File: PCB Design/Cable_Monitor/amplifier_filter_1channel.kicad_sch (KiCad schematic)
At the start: 6 parts, among them U7 MCP6002-xSN

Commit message: PCB Layout Update
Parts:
- renumbered C10 to C16, R18 to R15, R19 to R16, R20 to R17, R21 to R18, U7 to U5
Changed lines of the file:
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@@
   (symbol (lib_id "Amplifier_Operational:MCP6002-xSN") (at 93.98 50.8 0) (unit 1)
     (in_bom yes) (on_board yes) (dnp no) (fields_autoplaced)
-    (property "Reference" "U7" (at 93.98 40.64 0)
+    (property "Reference" "U5" (at 93.98 40.64 0)
       (effects (font (size 1.27 1.27)))
     )
@@
       (project "Cable_Monitor"
         (path "/1f276d59-ad9b-4e70-a842-f3b7e562eb9b/de01ffac-1f9d-4a03-9ae5-48822ed64956"
-          (reference "U7") (unit 1)
-        )
-        (path "/1f276d59-ad9b-4e70-a842-f3b7e562eb9b/dcec0d15-a185-46c1-b70e-bab38dd94215"
-          (reference "U1") (unit 1)
+          (reference "U5") (unit 1)
+        )
+        (path "/1f276d59-ad9b-4e70-a842-f3b7e562eb9b/dcec0d15-a185-46c1-b70e-bab38dd94215"
+          (reference "U6") (unit 1)
         )
       )
@@
   (symbol (lib_id "Device:R") (at 104.14 66.04 0) (unit 1)
     (in_bom yes) (on_board yes) (dnp no) (fields_autoplaced)
-    (property "Reference" "R19" (at 106.68 64.7699 0)
+    (property "Reference" "R16" (at 106.68 64.7699 0)
       (effects (font (size 1.27 1.27)) (justify left))
     )
@@
       (project "Cable_Monitor"
         (path "/1f276d59-ad9b-4e70-a842-f3b7e562eb9b/de01ffac-1f9d-4a03-9ae5-48822ed64956"
-          (reference "R19") (unit 1)
-        )
-        (path "/1f276d59-ad9b-4e70-a842-f3b7e562eb9b/dcec0d15-a185-46c1-b70e-bab38dd94215"
-          (reference "R2") (unit 1)
+          (reference "R16") (unit 1)
+        )
+        (path "/1f276d59-ad9b-4e70-a842-f3b7e562eb9b/dcec0d15-a185-46c1-b70e-bab38dd94215"
+          (reference "R20") (unit 1)
         )
       )
@@
   (symbol (lib_id "Device:R") (at 154.94 66.04 0) (unit 1)
     (in_bom yes) (on_board yes) (dnp no) (fields_autoplaced)
-    (property "Reference" "R21" (at 157.48 64.7699 0)
+    (property "Reference" "R18" (at 157.48 64.7699 0)
       (effects (font (size 1.27 1.27)) (justify left))
     )
@@
       (project "Cable_Monitor"
         (path "/1f276d59-ad9b-4e70-a842-f3b7e562eb9b/de01ffac-1f9d-4a03-9ae5-48822ed64956"
-          (reference "R21") (unit 1)
-        )
-        (path "/1f276d59-ad9b-4e70-a842-f3b7e562eb9b/dcec0d15-a185-46c1-b70e-bab38dd94215"
-          (reference "R4") (unit 1)
+          (reference "R18") (unit 1)
+        )
+        (path "/1f276d59-ad9b-4e70-a842-f3b7e562eb9b/dcec0d15-a185-46c1-b70e-bab38dd94215"
+          (reference "R22") (unit 1)
         )
       )
@@
   (symbol (lib_id "Amplifier_Operational:MCP6002-xSN") (at 144.78 50.8 0) (unit 2)
     (in_bom yes) (on_board yes) (dnp no) (fields_autoplaced)
-    (property "Reference" "U7" (at 144.78 40.64 0)
+    (property "Reference" "U5" (at 144.78 40.64 0)
       (effects (font (size 1.27 1.27)))
     )
@@
       (project "Cable_Monitor"
         (path "/1f276d59-ad9b-4e70-a842-f3b7e562eb9b/de01ffac-1f9d-4a03-9ae5-48822ed64956"
-          (reference "U7") (unit 2)
-        )
-        (path "/1f276d59-ad9b-4e70-a842-f3b7e562eb9b/dcec0d15-a185-46c1-b70e-bab38dd94215"
-          (reference "U1") (unit 2)
+          (reference "U5") (unit 2)
+        )
+        (path "/1f276d59-ad9b-4e70-a842-f3b7e562eb9b/dcec0d15-a185-46c1-b70e-bab38dd94215"
+          (reference "U6") (unit 2)
         )
       )
@@
   (symbol (lib_id "Device:C") (at 88.9 132.08 0) (unit 1)
     (in_bom yes) (on_board yes) (dnp no) (fields_autoplaced)
-    (property "Reference" "C10" (at 92.71 130.8099 0)
+    (property "Reference" "C16" (at 92.71 130.8099 0)
       (effects (font (size 1.27 1.27)) (justify left))
     )
@@
       (project "Cable_Monitor"
         (path "/1f276d59-ad9b-4e70-a842-f3b7e562eb9b/de01ffac-1f9d-4a03-9ae5-48822ed64956"
-          (reference "C10") (unit 1)
-        )
-        (path "/1f276d59-ad9b-4e70-a842-f3b7e562eb9b/dcec0d15-a185-46c1-b70e-bab38dd94215"
-          (reference "C2") (unit 1)
+          (reference "C16") (unit 1)
+        )
+        (path "/1f276d59-ad9b-4e70-a842-f3b7e562eb9b/dcec0d15-a185-46c1-b70e-bab38dd94215"
+          (reference "C17") (unit 1)
         )
       )
@@
   (symbol (lib_id "power:GND") (at 101.6 139.7 0) (unit 1)
     (in_bom yes) (on_board yes) (dnp no) (fields_autoplaced)
-    (property "Reference" "#PWR049" (at 101.6 146.05 0)
+    (property "Reference" "#PWR031" (at 101.6 146.05 0)
       (effects (font (size 1.27 1.27)) hide)
     )
@@
       (project "Cable_Monitor"
         (path "/1f276d59-ad9b-4e70-a842-f3b7e562eb9b/de01ffac-1f9d-4a03-9ae5-48822ed64956"
-          (reference "#PWR049") (unit 1)
-        )
-        (path "/1f276d59-ad9b-4e70-a842-f3b7e562eb9b/dcec0d15-a185-46c1-b70e-bab38dd94215"
-          (reference "#PWR013") (unit 1)
+          (reference "#PWR031") (unit 1)
+        )
+        (path "/1f276d59-ad9b-4e70-a842-f3b7e562eb9b/dcec0d15-a185-46c1-b70e-bab38dd94215"
+          (reference "#PWR035") (unit 1)
         )
       )
@@
   (symbol (lib_id "Device:R") (at 154.94 55.88 0) (unit 1)
     (in_bom yes) (on_board yes) (dnp no) (fields_autoplaced)
-    (property "Reference" "R20" (at 157.48 54.6099 0)
+    (property "Reference" "R17" (at 157.48 54.6099 0)
       (effects (font (size 1.27 1.27)) (justify left))
     )
@@
       (project "Cable_Monitor"
         (path "/1f276d59-ad9b-4e70-a842-f3b7e562eb9b/de01ffac-1f9d-4a03-9ae5-48822ed64956"
-          (reference "R20") (unit 1)
-        )
-        (path "/1f276d59-ad9b-4e70-a842-f3b7e562eb9b/dcec0d15-a185-46c1-b70e-bab38dd94215"
-          (reference "R3") (unit 1)
+          (reference "R17") (unit 1)
+        )
+        (path "/1f276d59-ad9b-4e70-a842-f3b7e562eb9b/dcec0d15-a185-46c1-b70e-bab38dd94215"
+          (reference "R21") (unit 1)
         )
       )
@@
   (symbol (lib_id "Device:R") (at 104.14 55.88 0) (unit 1)
     (in_bom yes) (on_board yes) (dnp no) (fields_autoplaced)
-    (property "Reference" "R18" (at 106.68 54.6099 0)
+    (property "Reference" "R15" (at 106.68 54.6099 0)
       (effects (font (size 1.27 1.27)) (justify left))
     )
@@
       (project "Cable_Monitor"
         (path "/1f276d59-ad9b-4e70-a842-f3b7e562eb9b/de01ffac-1f9d-4a03-9ae5-48822ed64956"
-          (reference "R18") (unit 1)
-        )
-        (path "/1f276d59-ad9b-4e70-a842-f3b7e562eb9b/dcec0d15-a185-46c1-b70e-bab38dd94215"
-          (reference "R1") (unit 1)
+          (reference "R15") (unit 1)
+        )
+        (path "/1f276d59-ad9b-4e70-a842-f3b7e562eb9b/dcec0d15-a185-46c1-b70e-bab38dd94215"
+          (reference "R19") (unit 1)
         )
       )
@@
   (symbol (lib_id "power:GND") (at 154.94 69.85 0) (unit 1)
     (in_bom yes) (on_board yes) (dnp no) (fields_autoplaced)
-    (property "Reference" "#PWR051" (at 154.94 76.2 0)
+    (property "Reference" "#PWR033" (at 154.94 76.2 0)
       (effects (font (size 1.27 1.27)) hide)
     )
@@
       (project "Cable_Monitor"
         (path "/1f276d59-ad9b-4e70-a842-f3b7e562eb9b/de01ffac-1f9d-4a03-9ae5-48822ed64956"
-          (reference "#PWR051") (unit 1)
-        )
-        (path "/1f276d59-ad9b-4e70-a842-f3b7e562eb9b/dcec0d15-a185-46c1-b70e-bab38dd94215"
-          (reference "#PWR015") (unit 1)
+          (reference "#PWR033") (unit 1)
+        )
+        (path "/1f276d59-ad9b-4e70-a842-f3b7e562eb9b/dcec0d15-a185-46c1-b70e-bab38dd94215"
+          (reference "#PWR037") (unit 1)
         )
       )
@@
   (symbol (lib_id "Amplifier_Operational:MCP6002-xSN") (at 104.14 132.08 0) (unit 3)
     (in_bom yes) (on_board yes) (dnp no) (fields_autoplaced)
-    (property "Reference" "U7" (at 102.87 130.8099 0)
+    (property "Reference" "U5" (at 102.87 130.8099 0)
       (effects (font (size 1.27 1.27)) (justify left))
     )
@@
       (project "Cable_Monitor"
         (path "/1f276d59-ad9b-4e70-a842-f3b7e562eb9b/de01ffac-1f9d-4a03-9ae5-48822ed64956"
-          (reference "U7") (unit 3)
-        )
-        (path "/1f276d59-ad9b-4e70-a842-f3b7e562eb9b/dcec0d15-a185-46c1-b70e-bab38dd94215"
-          (reference "U1") (unit 3)
+          (reference "U5") (unit 3)
+        )
+        (path "/1f276d59-ad9b-4e70-a842-f3b7e562eb9b/dcec0d15-a185-46c1-b70e-bab38dd94215"
+          (reference "U6") (unit 3)
         )
       )
@@
   (symbol (lib_id "power:+3V0") (at 101.6 124.46 0) (unit 1)
     (in_bom yes) (on_board yes) (dnp no)
-    (property "Reference" "#PWR048" (at 101.6 128.27 0)
+    (property "Reference" "#PWR030" (at 101.6 128.27 0)
       (effects (font (size 1.27 1.27)) hide)
     )
@@
       (project "Cable_Monitor"
         (path "/1f276d59-ad9b-4e70-a842-f3b7e562eb9b/de01ffac-1f9d-4a03-9ae5-48822ed64956"
-          (reference "#PWR048") (unit 1)
-        )
-        (path "/1f276d59-ad9b-4e70-a842-f3b7e562eb9b/dcec0d15-a185-46c1-b70e-bab38dd94215"
-          (reference "#PWR012") (unit 1)
+          (reference "#PWR030") (unit 1)
+        )
+        (path "/1f276d59-ad9b-4e70-a842-f3b7e562eb9b/dcec0d15-a185-46c1-b70e-bab38dd94215"
+          (reference "#PWR034") (unit 1)
         )
       )
@@
   (symbol (lib_id "power:GND") (at 104.14 69.85 0) (unit 1)
     (in_bom yes) (on_board yes) (dnp no) (fields_autoplaced)
-    (property "Reference" "#PWR050" (at 104.14 76.2 0)
+    (property "Reference" "#PWR032" (at 104.14 76.2 0)
       (effects (font (size 1.27 1.27)) hide)
     )
@@
       (project "Cable_Monitor"
         (path "/1f276d59-ad9b-4e70-a842-f3b7e562eb9b/de01ffac-1f9d-4a03-9ae5-48822ed64956"
-          (reference "#PWR050") (unit 1)
-        )
-        (path "/1f276d59-ad9b-4e70-a842-f3b7e562eb9b/dcec0d15-a185-46c1-b70e-bab38dd94215"
-          (reference "#PWR014") (unit 1)
-        )
-      )
+          (reference "#PWR032") (unit 1)
+        )
+        (path "/1f276d59-ad9b-4e70-a842-f3b7e562eb9b/dcec0d15-a185-46c1-b70e-bab38dd94215"
+          (reference "#PWR036") (unit 1)
+        )
+      )

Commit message: PCB Design Update
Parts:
- removed R15: 10k, Resistor_SMD:R_0805_2012Metric_Pad1.20x1.40mm_HandSolder, symbol Device:R
- removed R16: 1k, Resistor_SMD:R_0805_2012Metric_Pad1.20x1.40mm_HandSolder, symbol Device:R
- removed unit 1 of U5
- added C16, C17, C22, C23: 0.16uF, symbol Device:C
- added C18, C19, C20, C21: 10uF, symbol Device:C
- added R11, R12, R19, R20: 10k, symbol Device:R
- added R13, R14: 100k, symbol Device:R
- added R17: 1M, Resistor_SMD:R_0805_2012Metric_Pad1.20x1.40mm_HandSolder, symbol Device:R
- added R18: 1k, Resistor_SMD:R_0805_2012Metric_Pad1.20x1.40mm_HandSolder, symbol Device:R
- added unit 2 of U7
- R15: renamed from R17; value 12k -> 1M
- renumbered C16 to C15, R18 to R16, U5 to U7
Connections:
- net GND: now also C16.1, C17.1, C20.2, C21.2, C22.2, C23.2; no longer R16.2
- net at R15.2, R16.1: now also U7.2 (-); no longer U7.6 (-)
- net out: no longer names the net of R15.1
- net out: now also U7.1, R19.1; no longer U7.7
- new net: C20.1, R16.2
- new net: C19.2, R14.1, U7.5 (+)
- new net: R17.2, R18.1, U7.6 (-)
- new net: R17.1, R20.1, U7.7
- new net: C16.2, C18.1, R11.2
- new net: C17.2, C19.1, R12.2
- new net: C18.2, R13.1, U7.3 (+)
- new net: C21.1, R18.2
- new net VGND: R13.2, R14.2
- new net in_left: R11.1
- new net in_right: R12.1
- new net out_left: C22.1, R19.2
- new net out_right: C23.1, R20.2
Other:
- note added: "1.5V"
- moved on the sheet: C15, R15, R16, U7A, U7C

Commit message: Letzte Anpassungen am Schema
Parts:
- renumbered R11 to R14, R12 to R15, R13 to R16, R14 to R17, R15 to R18, R16 to R19, R17 to R20, R18 to R21, R19 to R22, R20 to R23

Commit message: Schema Updates, bald Fertig
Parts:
- added TP13: HS_left_VGND, TestPoint:TestPoint_Loop_D2.60mm_Drill1.6mm_Beaded, symbol Connector:TestPoint
- added TP13: HS_right_VGND, TestPoint:TestPoint_Loop_D2.60mm_Drill1.6mm_Beaded, symbol Connector:TestPoint
- C16, C17, C18, C19, C20, C21, C22, C23: footprint (none) -> Capacitor_SMD:C_0805_2012Metric_Pad1.18x1.45mm_HandSolder
- R14, R15, R16, R17, R22, R23: footprint (none) -> Resistor_SMD:R_0805_2012Metric_Pad1.20x1.40mm_HandSolder
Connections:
- net at C19.2, R17.1, U7.5 (+): now also TP13.1
- net at C18.2, R16.1, U7.3 (+): now also TP13.1
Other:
- moved on the sheet: R17

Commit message: Update
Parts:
- renumbered R14 to R17, R15 to R18, R16 to R19, R17 to R20, R18 to R21, R19 to R22, R20 to R23, R21 to R24, R22 to R25, R23 to R26
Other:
- note added: "Filtering and Amplification used for Hall-Sensors. The Hall-Sensors will be used to measure a magnetic Field and thus allow us to calculate a current."
- note added: "Supply Voltage for OP-Amp"
- note removed: "Some often used components are included here. Delete the components that are not used. Copy the components that are needed more than once."
- note removed: "Use this template if two opamps are used for better amplification and filtering. As dual opamps are used, one channel only can be handled by this sheet."
- company: hhrt@zhaw.ch -> ZHAW
- title: Amplifiers and Filters -> Amplifiers and Filters for Hall-Sensor

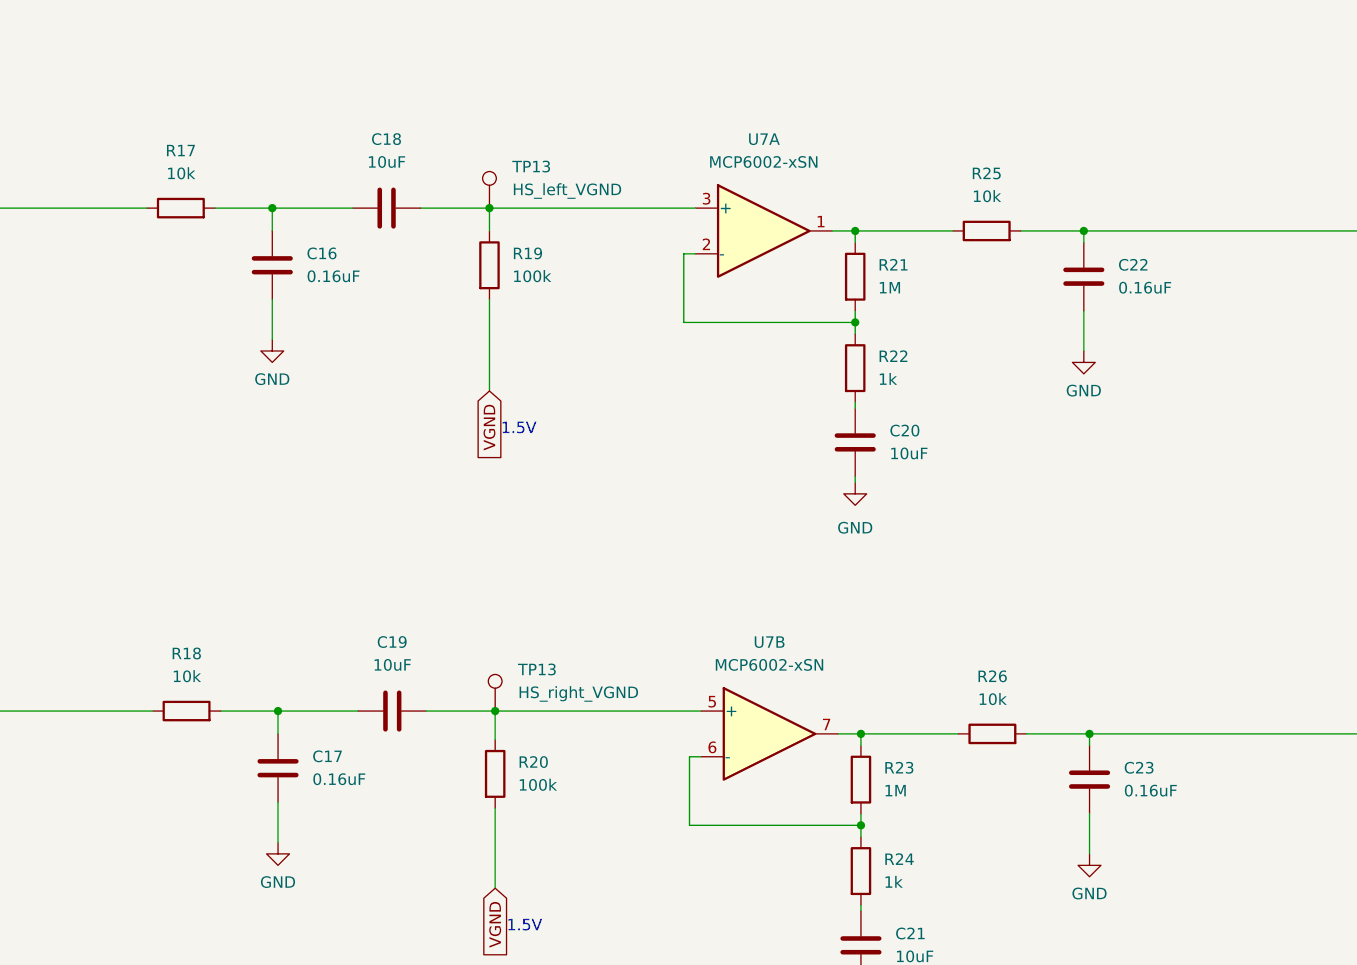
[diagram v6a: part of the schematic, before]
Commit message: Schema PDF Export
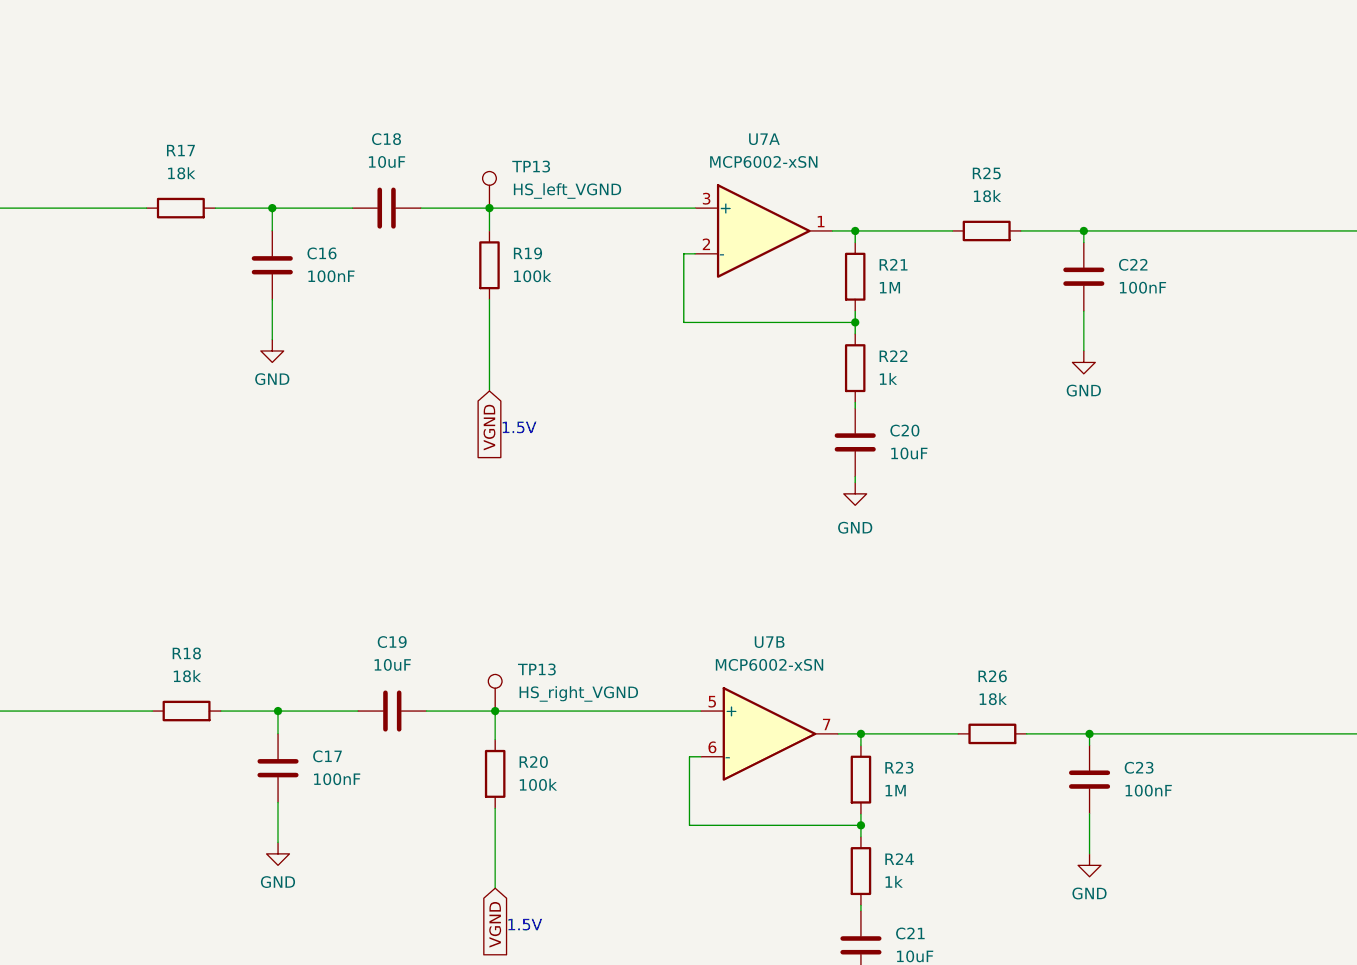
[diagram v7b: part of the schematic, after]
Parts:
- C16, C17, C22, C23: value 0.16uF -> 100nF
- R17, R18, R25, R26: value 10k -> 18k
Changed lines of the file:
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@@
       (effects (font (size 1.27 1.27)) (justify left))
     )
-    (property "Value" "0.16uF" (at 184.785 115.57 0)
+    (property "Value" "100nF" (at 184.785 115.57 0)
       (effects (font (size 1.27 1.27)) (justify left))
     )
@@
       (effects (font (size 1.27 1.27)) (justify right))
     )
-    (property "Value" "0.16uF" (at 93.98 58.42 0)
+    (property "Value" "100nF" (at 93.98 58.42 0)
       (effects (font (size 1.27 1.27)) (justify right))
     )
@@
       (effects (font (size 1.27 1.27)))
     )
-    (property "Value" "10k" (at 80.645 102.87 90)
+    (property "Value" "18k" (at 80.645 102.87 90)
       (effects (font (size 1.27 1.27)))
     )
@@
       (effects (font (size 1.27 1.27)) (justify left))
     )
-    (property "Value" "0.16uF" (at 184.15 59.69 0)
+    (property "Value" "100nF" (at 184.15 59.69 0)
       (effects (font (size 1.27 1.27)) (justify left))
     )
@@
       (effects (font (size 1.27 1.27)))
     )
-    (property "Value" "10k" (at 80.01 46.99 90)
+    (property "Value" "18k" (at 80.01 46.99 90)
       (effects (font (size 1.27 1.27)))
     )
@@
       (effects (font (size 1.27 1.27)))
     )
-    (property "Value" "10k" (at 170.18 105.41 90)
+    (property "Value" "18k" (at 170.18 105.41 90)
       (effects (font (size 1.27 1.27)))
     )
@@
       (effects (font (size 1.27 1.27)) (justify right))
     )
-    (property "Value" "0.16uF" (at 94.615 114.3 0)
+    (property "Value" "100nF" (at 94.615 114.3 0)
       (effects (font (size 1.27 1.27)) (justify right))
     )
@@
       (effects (font (size 1.27 1.27)))
     )
-    (property "Value" "10k" (at 169.545 49.53 90)
-      (effects (font (size 1.27 1.27)))
-    )
+    (property "Value" "18k" (at 169.545 49.53 90)
+      (effects (font (size 1.27 1.27)))
+    )
